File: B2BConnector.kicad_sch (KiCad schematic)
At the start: 6 parts, among them J5 FX23L-80P-0.5SV10, J6 FX23L-80P-0.5SV10, Q1 Q_NMOS_GSD

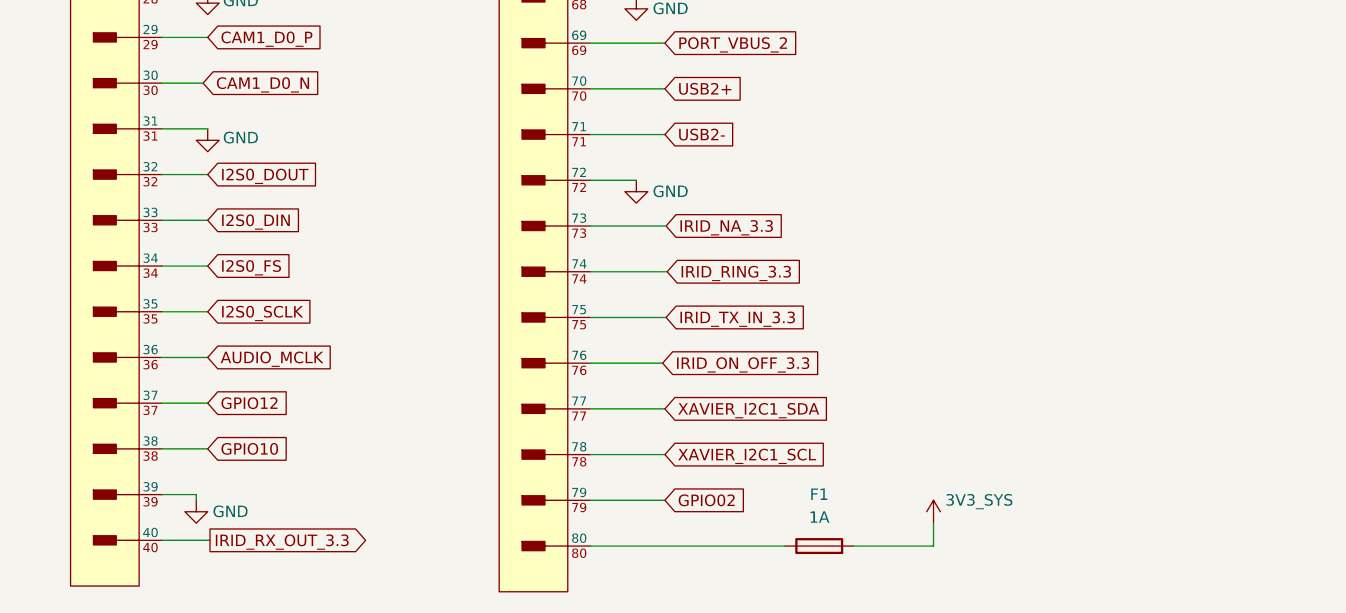
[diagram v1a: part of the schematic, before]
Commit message: updates for Rev1B boards, pinout changes on J5 and J8
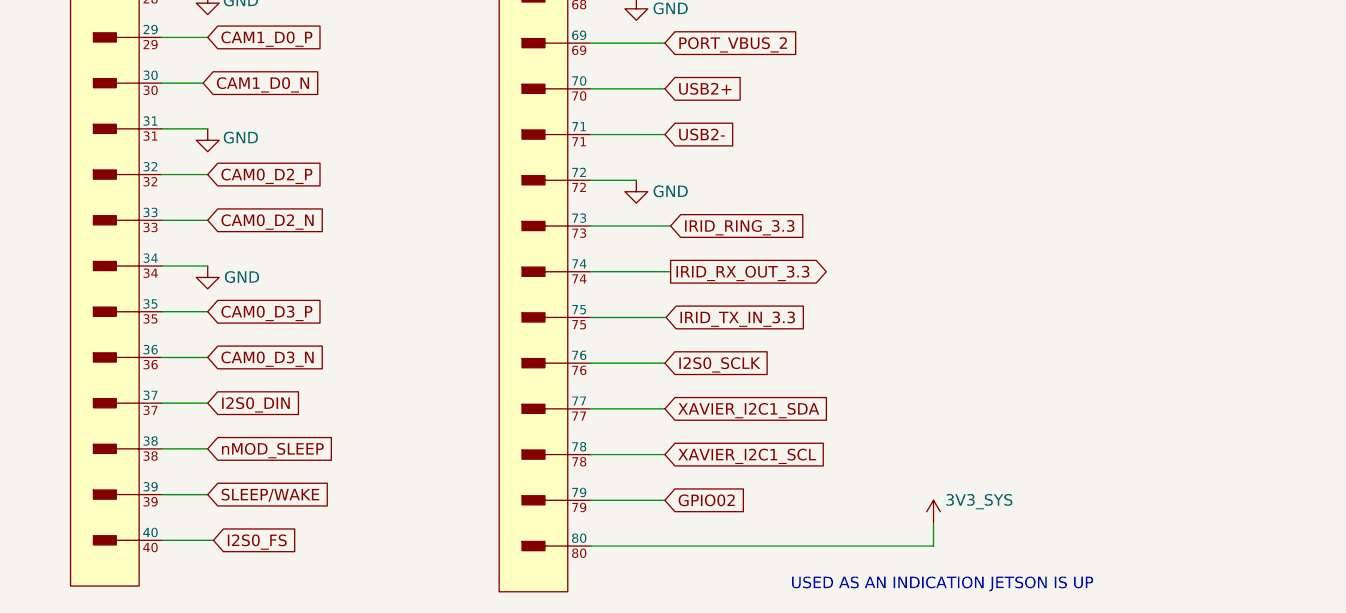
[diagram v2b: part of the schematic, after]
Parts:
- removed F1: 1A, Fuse:Fuse_0603_1608Metric, symbol Device:Fuse
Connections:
- net GPIO12 is gone; now on net I2S0_DIN: J5.37
- net IRID_NA_3.3 is gone; now on net IRID_RING_3.3: J5.73
- net IRID_ON_OFF_3.3 is gone; now on net I2S0_SCLK: J5.76
- net 3V3_SYS: now also J5.80
- net GND: now also J5.34; no longer J5.39
- net I2S0_DIN: no longer J5.33
- net I2S0_FS: now also J5.40; no longer J5.34
- net I2S0_SCLK: no longer J5.35
- net IRID_RING_3.3: no longer J5.74
- net IRID_RX_OUT_3.3: now also J5.74; no longer J5.40
- net AUDIO_MCLK renamed CAM0_D3_N
- net GPIO10 renamed nMOD_SLEEP
- net I2S0_DOUT renamed CAM0_D2_P
- new net CAM0_D2_N: J5.33
- new net CAM0_D3_P: J5.35
- new net SLEEP/WAKE: J5.39
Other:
- note added: "USED AS AN INDICATION JETSON IS UP"
